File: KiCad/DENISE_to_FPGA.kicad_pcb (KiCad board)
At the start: 2 copper layers, 80 x 29.5 mm, 11 parts, among them J1 Conn_01x02, U1 Denise_Socket, U2 Denise_MB_PinHeader, U3 LM1117-3.3

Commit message: New design, more routing done
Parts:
- removed the REF** at (133.3, 98.4)
- added J2: Conn_01x40, Connector_FFC-FPC:Hirose_FH12-40S-0.5SH_1x40-1MP_P0.50mm_Horizontal, F.Cu at (200.5, 90.4)
- added REF**: OSHW-Logo_11.4x12mm_Copper, Symbol:OSHW-Logo_11.4x12mm_Copper, B.Cu at (198.4, 90.6)
- added U4: Denise_MB_PinHeader, DENISE_to_FPGA:DIP-48_W15.24mm_Socket_LongPads, F.Cu at (188.0, 88.1)
- U1: value Denise_Socket -> 74LVC245A; footprint Package_DIP:DIP-48_W15.24mm_Socket_LongPads -> Package_SO:TSSOP-20_4.4x6.5mm_P0.65mm
- U2: value Denise_MB_PinHeader -> 74LVC245A; footprint Package_DIP:DIP-48_W15.24mm_LongPads -> Package_SO:TSSOP-20_4.4x6.5mm_P0.65mm
- moved C4 70.5 mm to (145.2, 91.1)
- moved U3 63.0 mm to (137.1, 96.5), turned to 0 degrees
- moved C2 58.4 mm to (146.1, 95.6)
- moved C1 57.4 mm to (136.8, 91.7), turned to 0 degrees
- moved C3 53.0 mm to (153.7, 95.1)
- moved U1 48.0 mm to (143.5, 95.8), turned to 0 degrees
- moved C5 42.6 mm to (179.5, 94.6), turned to 180 degrees
- moved U2 17.6 mm to (172.7, 97.0), turned to 0 degrees
- moved J1 3.99 mm to (195.6, 103.4)
- moved REF** 2.67 mm to (133.3, 95.8)
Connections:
- U1 pad 1: D6 -> 3V3
- U1 pad 10: RGA8 -> GND
- U1 pad 11: RGA7 -> G3_3V3
- U1 pad 12: RGA6 -> G2_3V3
- U1 pad 13: RGA5 -> G1_3V3
- U1 pad 14: RGA4 -> G0_3V3
- U1 pad 15: RGA3 -> R3_3V3
- U1 pad 16: RGA2 -> R2_3V3
- U1 pad 17: RGA1 -> R1_3V3
- U1 pad 18: BURST -> R0_3V3
- U1 pad 19: VCC -> GND
- U1 pad 2: D5 -> R0
- U1 pad 20: R0 -> 3V3
- U1 pad 3: D4 -> R1
- U1 pad 4: D3 -> R2
- U1 pad 5: D2 -> R3
- U1 pad 6: D1 -> G0
- U1 pad 7: D0 -> G1
- U1 pad 8: M1H -> G2
- U1 pad 9: M0H -> G3
- U2 pad 1: D6 -> 3V3
- U2 pad 10: RGA8 -> GND
- U2 pad 11: RGA7 -> C7M_3V3
- U2 pad 12: RGA6 -> CDAC_3V3
- U2 pad 13: RGA5 -> PIXELSW_3V3
- U2 pad 14: RGA4 -> CSYNC_3V3
- U2 pad 15: RGA3 -> B3_3V3
- U2 pad 16: RGA2 -> B2_3V3
- U2 pad 17: RGA1 -> B1_3V3
- U2 pad 18: BURST -> B0_3V3
- U2 pad 19: VCC -> GND
- U2 pad 2: D5 -> B0
- U2 pad 20: R0 -> 3V3
- U2 pad 3: D4 -> B1
- U2 pad 4: D3 -> B2
- U2 pad 5: D2 -> B3
- U2 pad 6: D1 -> CSYNC
- U2 pad 7: D0 -> PIXELSW
- U2 pad 8: M1H -> CDAC
- U2 pad 9: M0H -> C7M
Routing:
- net 3V3: track 13.2 -> 76.4 mm, vias 0 -> 5
- net G0: track 69.6 -> 9.59 mm, vias 0 -> 1
- net G1: track 67.1 -> 8.87 mm, vias 0 -> 1
- net G2: track 64.5 -> 7.59 mm, vias 0 -> 1
- net G3: track 65.2 -> 8.40 mm, vias 0 -> 1
- net VCC: track 69.5 -> 13.0 mm
- net R3: track 68.3 -> 11.8 mm
- net R3_3V3: track 0.00 -> 56.4 mm
- net R2_3V3: track 0.00 -> 56.4 mm
- net R1_3V3: track 0.00 -> 56.3 mm
- net R0_3V3: track 0.00 -> 56.2 mm
- net G3_3V3: track 0.00 -> 55.8 mm
- net G2_3V3: track 0.00 -> 55.8 mm
- net G1_3V3: track 0.00 -> 55.7 mm
- net G0_3V3: track 0.00 -> 55.6 mm
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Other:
- board size 80 x 29.5 mm -> 78.5 x 29.5 mm
- rule pad_to_mask_clearance: 0.05 -> 0
- board text added: "CDAC"
- board text added: "DENISE to FPGA"
- board text added: "Rev. A"
- board text removed: "DENISE to FPGA Rev. A"

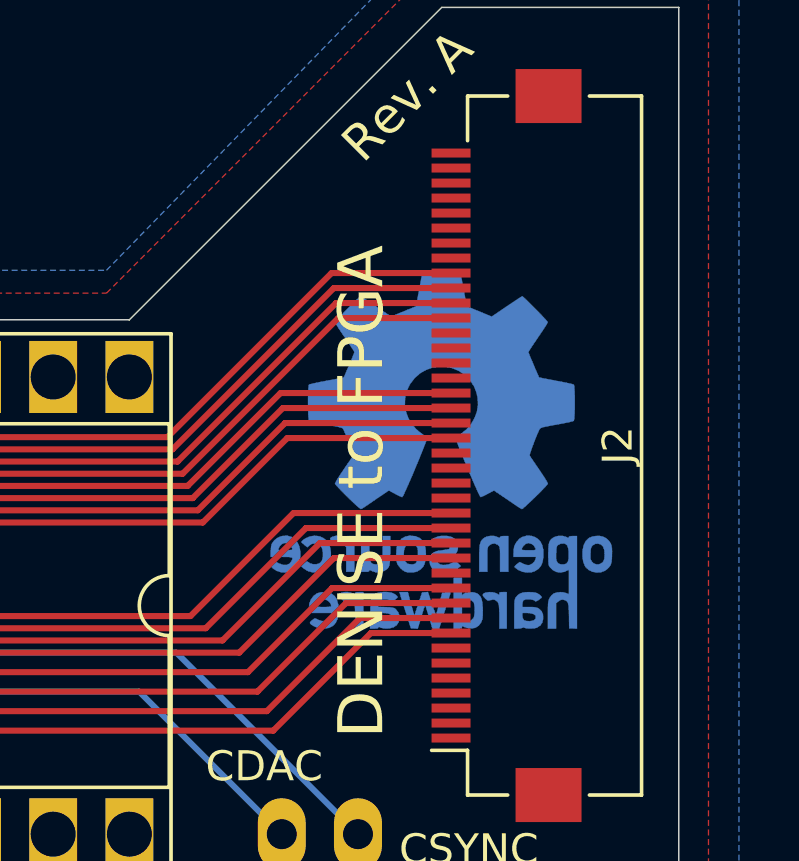
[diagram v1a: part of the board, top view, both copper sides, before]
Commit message: Fixed GND-routing on FPC-conn
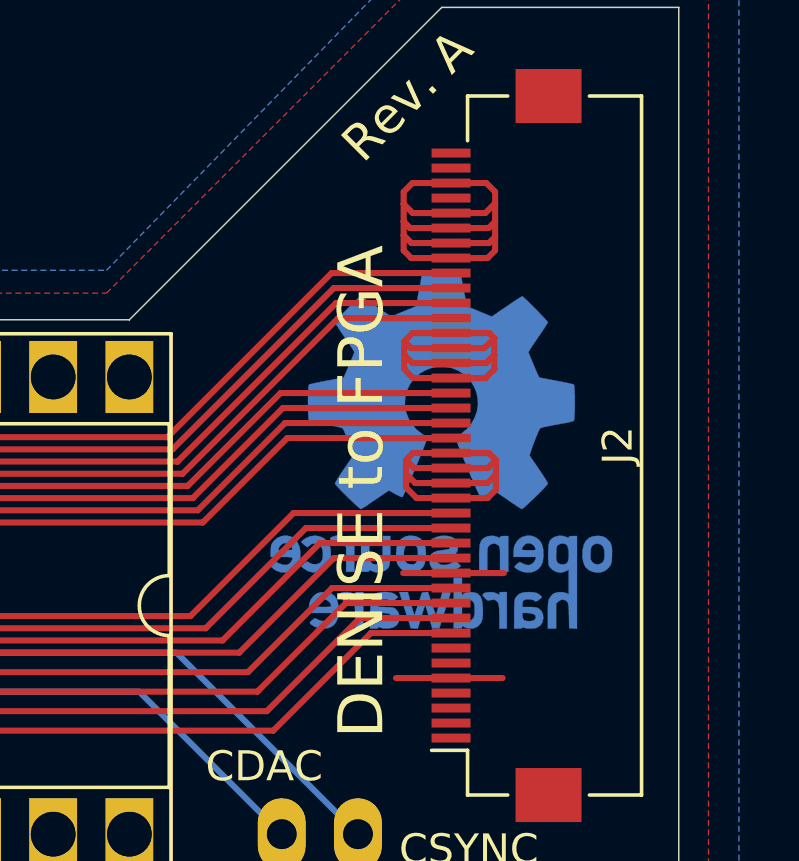
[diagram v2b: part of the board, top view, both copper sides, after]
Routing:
- net GND: track 0.00 -> 56.8 mm
